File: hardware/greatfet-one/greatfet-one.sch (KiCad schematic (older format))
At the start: 99 parts, among them J1 NEIGHBOR1, J2 NEIGHBOR2, J3 USB-MICRO-B-SHIELDED, J4 USB-MICRO-B-SHIELDED, J5 JTAG, J6 POWER, J7 BONUS_ROW, SW1 DFU, SW2 RESET, U1 LPC4330FBD144, U2 W25Q16DV, U3 AP7333, U4 IP4220CZ6, U5 AP2553W6-7, X1 MCU_XTAL, X2 RTC_XTAL

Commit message: GreatFET One: replaced D5 with a part with lower forward voltage to maximize the usefulness of +5V for USB1 and neighbors
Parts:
- D5: footprint gsg-modules:B140-13-F -> gsg-modules:SOD128; Description DIODE SCHOTTKY 40V 1A SMA -> DIODE SCHOTTKY 30V 5A SOD128; Manufacturer Diodes Inc. -> NXP; Part Number B140-13-F -> PMEG3050EP,115
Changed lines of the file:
@@
 F 0 "D5" H 2500 6300 50  0000 C CNN
 F 1 "VBUS_DIODE" H 2500 6100 50  0000 C CNN
-F 2 "gsg-modules:B140-13-F" H 2500 6200 60  0001 C CNN
+F 2 "gsg-modules:SOD128" H 2500 6200 60  0001 C CNN
 F 3 "" H 2500 6200 60  0000 C CNN
-F 4 "Diodes Inc." H 2500 6200 60  0001 C CNN "Manufacturer"
-F 5 "B140-13-F" H 2500 6200 60  0001 C CNN "Part Number"
-F 6 "DIODE SCHOTTKY 40V 1A SMA" H 2500 6200 60  0001 C CNN "Description"
+F 4 "NXP" H 2500 6200 60  0001 C CNN "Manufacturer"
+F 5 "PMEG3050EP,115" H 2500 6200 60  0001 C CNN "Part Number"
+F 6 "DIODE SCHOTTKY 30V 5A SOD128 " H 2500 6200 60  0001 C CNN "Description"
 	1    2500 6200
 	1    0    0    -1

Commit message: GreatFET One: corrected part numbers for 18k resistors
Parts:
- R22, R26: Description RES SMD 10K OHM 5% 1/10W 0603 -> RES SMD 18K OHM 5% 1/10W 0603; Part Number RC0603JR-0710KL -> RC0603JR-0718KL
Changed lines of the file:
@@
 F 3 "" H 13200 4950 30  0000 C CNN
 F 4 "Yageo" H 13200 4950 60  0001 C CNN "Manufacturer"
-F 5 "RC0603JR-0710KL" H 13200 4950 60  0001 C CNN "Part Number"
-F 6 "RES SMD 10K OHM 5% 1/10W 0603" H 13200 4950 60  0001 C CNN "Description"
+F 5 "RC0603JR-0718KL" H 13200 4950 60  0001 C CNN "Part Number"
+F 6 "RES SMD 18K OHM 5% 1/10W 0603" H 13200 4950 60  0001 C CNN "Description"
 	1    13200 4950
 	-1   0    0    1
@@
 F 3 "" H 2800 7250 30  0000 C CNN
 F 4 "Yageo" H 2800 7250 60  0001 C CNN "Manufacturer"
-F 5 "RC0603JR-0710KL" H 2800 7250 60  0001 C CNN "Part Number"
-F 6 "RES SMD 10K OHM 5% 1/10W 0603" H 2800 7250 60  0001 C CNN "Description"
+F 5 "RC0603JR-0718KL" H 2800 7250 60  0001 C CNN "Part Number"
+F 6 "RES SMD 18K OHM 5% 1/10W 0603" H 2800 7250 60  0001 C CNN "Description"
 	1    2800 7250
 	-1   0    0    1

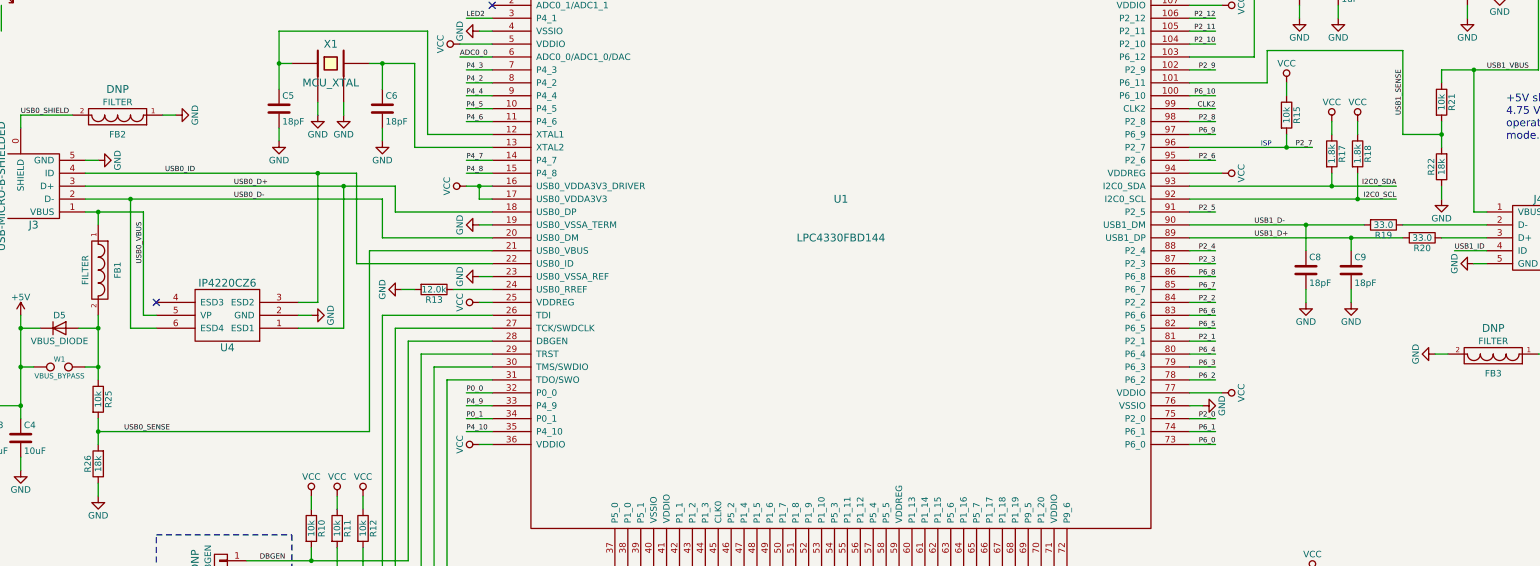
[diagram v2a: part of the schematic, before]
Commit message: GreatFET One: Changed resistor values to fix voltage dividers for USB0 and USB1 VBUS sensing.
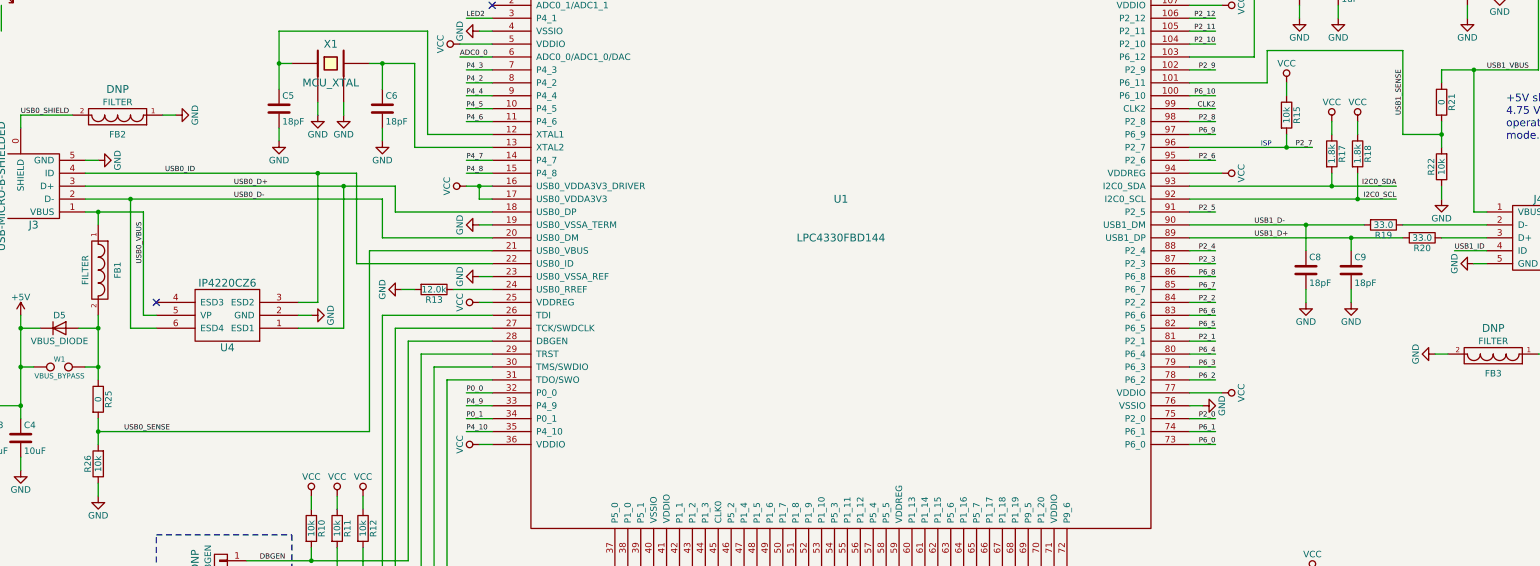
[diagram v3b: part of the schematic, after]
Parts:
- R21, R25: value 10k -> 0; Description RES 10K OHM 1/10W 5% 0603 SMD -> RES SMD 0.0OHM JUMPER 1/10W 0603; Manufacturer Panasonic -> Yageo; Part Number ERJ-3GEYJ103V -> RC0603JR-070RL
- R22, R26: value 18k -> 10k; Description RES SMD 18K OHM 5% 1/10W 0603 -> RES 10K OHM 1/10W 5% 0603 SMD; Manufacturer Yageo -> Panasonic; Part Number RC0603JR-0718KL -> ERJ-3GEYJ103V
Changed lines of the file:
@@
 P 13200 4950
 F 0 "R22" V 13280 4950 50  0000 C CNN
-F 1 "18k" V 13200 4950 50  0000 C CNN
+F 1 "10k" V 13200 4950 50  0000 C CNN
 F 2 "gsg-modules:0603" V 13130 4950 30  0001 C CNN
 F 3 "" H 13200 4950 30  0000 C CNN
-F 4 "Yageo" H 13200 4950 60  0001 C CNN "Manufacturer"
-F 5 "RC0603JR-0718KL" H 13200 4950 60  0001 C CNN "Part Number"
-F 6 "RES SMD 18K OHM 5% 1/10W 0603" H 13200 4950 60  0001 C CNN "Description"
+F 4 "Panasonic" H 13200 4950 60  0001 C CNN "Manufacturer"
+F 5 "ERJ-3GEYJ103V" H 13200 4950 60  0001 C CNN "Part Number"
+F 6 "RES 10K OHM 1/10W 5% 0603 SMD" H 13200 4950 60  0001 C CNN "Description"
 	1    13200 4950
 	-1   0    0    1
@@
 P 13200 4450
 F 0 "R21" V 13280 4450 50  0000 C CNN
-F 1 "10k" V 13200 4450 50  0000 C CNN
+F 1 "0" V 13200 4450 50  0000 C CNN
 F 2 "gsg-modules:0603" V 13130 4450 30  0001 C CNN
 F 3 "" H 13200 4450 30  0000 C CNN
-F 4 "Panasonic" H 13200 4450 60  0001 C CNN "Manufacturer"
-F 5 "ERJ-3GEYJ103V" H 13200 4450 60  0001 C CNN "Part Number"
-F 6 "RES 10K OHM 1/10W 5% 0603 SMD" H 13200 4450 60  0001 C CNN "Description"
+F 4 "Yageo" H 13200 4450 60  0001 C CNN "Manufacturer"
+F 5 "RC0603JR-070RL" H 13200 4450 60  0001 C CNN "Part Number"
+F 6 "RES SMD 0.0OHM JUMPER 1/10W 0603" H 13200 4450 60  0001 C CNN "Description"
 	1    13200 4450
 	1    0    0    -1
@@
 P 2800 6750
 F 0 "R25" V 2880 6750 50  0000 C CNN
-F 1 "10k" V 2800 6750 50  0000 C CNN
+F 1 "0" V 2800 6750 50  0000 C CNN
 F 2 "gsg-modules:0603" V 2730 6750 30  0001 C CNN
 F 3 "" H 2800 6750 30  0000 C CNN
-F 4 "Panasonic" H 2800 6750 60  0001 C CNN "Manufacturer"
-F 5 "ERJ-3GEYJ103V" H 2800 6750 60  0001 C CNN "Part Number"
-F 6 "RES 10K OHM 1/10W 5% 0603 SMD" H 2800 6750 60  0001 C CNN "Description"
+F 4 "Yageo" H 2800 6750 60  0001 C CNN "Manufacturer"
+F 5 "RC0603JR-070RL" H 2800 6750 60  0001 C CNN "Part Number"
+F 6 "RES SMD 0.0OHM JUMPER 1/10W 0603" H 2800 6750 60  0001 C CNN "Description"
 	1    2800 6750
 	1    0    0    -1
@@
 P 2800 7250
 F 0 "R26" V 2880 7250 50  0000 C CNN
-F 1 "18k" V 2800 7250 50  0000 C CNN
+F 1 "10k" V 2800 7250 50  0000 C CNN
 F 2 "gsg-modules:0603" V 2730 7250 30  0001 C CNN
 F 3 "" H 2800 7250 30  0000 C CNN
-F 4 "Yageo" H 2800 7250 60  0001 C CNN "Manufacturer"
-F 5 "RC0603JR-0718KL" H 2800 7250 60  0001 C CNN "Part Number"
-F 6 "RES SMD 18K OHM 5% 1/10W 0603" H 2800 7250 60  0001 C CNN "Description"
+F 4 "Panasonic" H 2800 7250 60  0001 C CNN "Manufacturer"
+F 5 "ERJ-3GEYJ103V" H 2800 7250 60  0001 C CNN "Part Number"
+F 6 "RES 10K OHM 1/10W 5% 0603 SMD" H 2800 7250 60  0001 C CNN "Description"
 	1    2800 7250
 	-1   0    0    1

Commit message: Restored VBUS voltage dividers which work correctly now that we learned how to turn off VBUS discharge in the microcontroller.
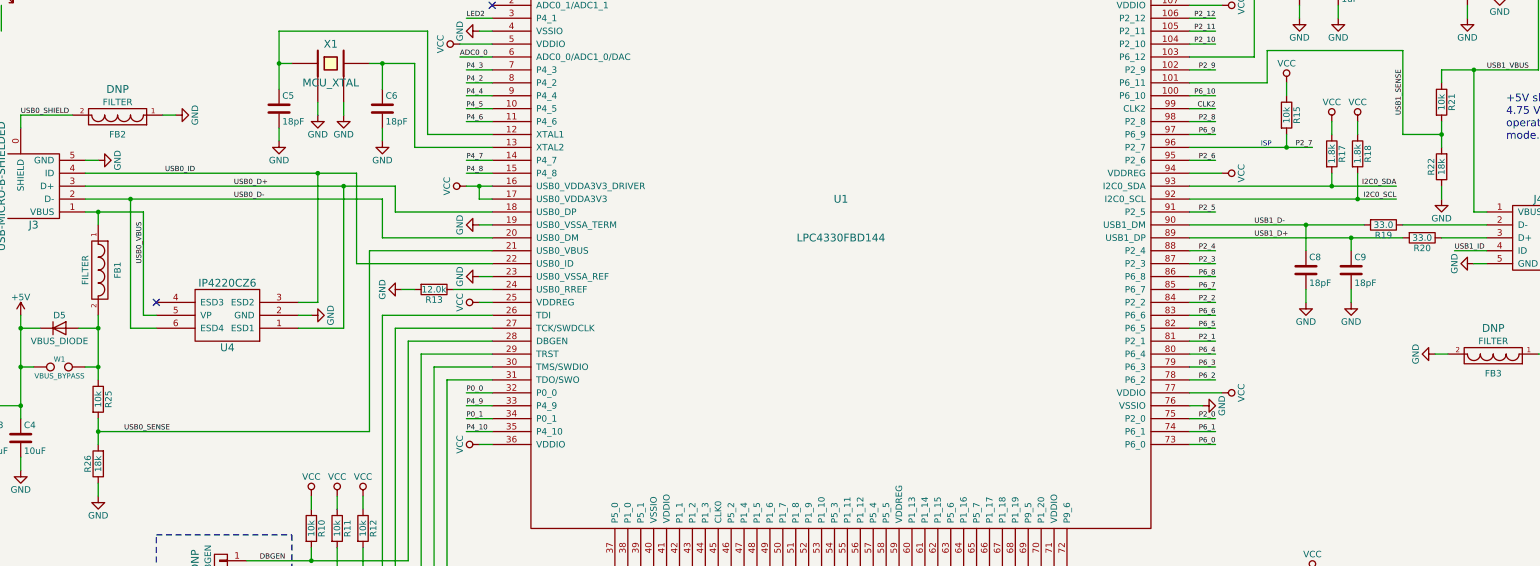
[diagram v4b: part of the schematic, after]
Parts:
- R21, R25: value 0 -> 10k; Description RES SMD 0.0OHM JUMPER 1/10W 0603 -> RES 10K OHM 1/10W 5% 0603 SMD; Manufacturer Yageo -> Panasonic; Part Number RC0603JR-070RL -> ERJ-3GEYJ103V
- R22, R26: value 10k -> 18k; Description RES 10K OHM 1/10W 5% 0603 SMD -> RES SMD 18K OHM 5% 1/10W 0603; Manufacturer Panasonic -> Yageo; Part Number ERJ-3GEYJ103V -> RC0603JR-0718KL
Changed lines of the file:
@@
 P 13200 4950
 F 0 "R22" V 13280 4950 50  0000 C CNN
-F 1 "10k" V 13200 4950 50  0000 C CNN
+F 1 "18k" V 13200 4950 50  0000 C CNN
 F 2 "gsg-modules:0603" V 13130 4950 30  0001 C CNN
 F 3 "" H 13200 4950 30  0000 C CNN
-F 4 "Panasonic" H 13200 4950 60  0001 C CNN "Manufacturer"
-F 5 "ERJ-3GEYJ103V" H 13200 4950 60  0001 C CNN "Part Number"
-F 6 "RES 10K OHM 1/10W 5% 0603 SMD" H 13200 4950 60  0001 C CNN "Description"
+F 4 "Yageo" H 13200 4950 60  0001 C CNN "Manufacturer"
+F 5 "RC0603JR-0718KL" H 13200 4950 60  0001 C CNN "Part Number"
+F 6 "RES SMD 18K OHM 5% 1/10W 0603" H 13200 4950 60  0001 C CNN "Description"
 	1    13200 4950
 	-1   0    0    1
@@
 P 13200 4450
 F 0 "R21" V 13280 4450 50  0000 C CNN
-F 1 "0" V 13200 4450 50  0000 C CNN
+F 1 "10k" V 13200 4450 50  0000 C CNN
 F 2 "gsg-modules:0603" V 13130 4450 30  0001 C CNN
 F 3 "" H 13200 4450 30  0000 C CNN
-F 4 "Yageo" H 13200 4450 60  0001 C CNN "Manufacturer"
-F 5 "RC0603JR-070RL" H 13200 4450 60  0001 C CNN "Part Number"
-F 6 "RES SMD 0.0OHM JUMPER 1/10W 0603" H 13200 4450 60  0001 C CNN "Description"
+F 4 "Panasonic" H 13200 4450 60  0001 C CNN "Manufacturer"
+F 5 "ERJ-3GEYJ103V" H 13200 4450 60  0001 C CNN "Part Number"
+F 6 "RES 10K OHM 1/10W 5% 0603 SMD" H 13200 4450 60  0001 C CNN "Description"
 	1    13200 4450
 	1    0    0    -1
@@
 P 2800 6750
 F 0 "R25" V 2880 6750 50  0000 C CNN
-F 1 "0" V 2800 6750 50  0000 C CNN
+F 1 "10k" V 2800 6750 50  0000 C CNN
 F 2 "gsg-modules:0603" V 2730 6750 30  0001 C CNN
 F 3 "" H 2800 6750 30  0000 C CNN
-F 4 "Yageo" H 2800 6750 60  0001 C CNN "Manufacturer"
-F 5 "RC0603JR-070RL" H 2800 6750 60  0001 C CNN "Part Number"
-F 6 "RES SMD 0.0OHM JUMPER 1/10W 0603" H 2800 6750 60  0001 C CNN "Description"
+F 4 "Panasonic" H 2800 6750 60  0001 C CNN "Manufacturer"
+F 5 "ERJ-3GEYJ103V" H 2800 6750 60  0001 C CNN "Part Number"
+F 6 "RES 10K OHM 1/10W 5% 0603 SMD" H 2800 6750 60  0001 C CNN "Description"
 	1    2800 6750
 	1    0    0    -1
@@
 P 2800 7250
 F 0 "R26" V 2880 7250 50  0000 C CNN
-F 1 "10k" V 2800 7250 50  0000 C CNN
+F 1 "18k" V 2800 7250 50  0000 C CNN
 F 2 "gsg-modules:0603" V 2730 7250 30  0001 C CNN
 F 3 "" H 2800 7250 30  0000 C CNN
-F 4 "Panasonic" H 2800 7250 60  0001 C CNN "Manufacturer"
-F 5 "ERJ-3GEYJ103V" H 2800 7250 60  0001 C CNN "Part Number"
-F 6 "RES 10K OHM 1/10W 5% 0603 SMD" H 2800 7250 60  0001 C CNN "Description"
+F 4 "Yageo" H 2800 7250 60  0001 C CNN "Manufacturer"
+F 5 "RC0603JR-0718KL" H 2800 7250 60  0001 C CNN "Part Number"
+F 6 "RES SMD 18K OHM 5% 1/10W 0603" H 2800 7250 60  0001 C CNN "Description"
 	1    2800 7250
 	-1   0    0    1

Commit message: updated from discontinued W25Q16DVSSIG to compatible W25Q16JVSSIQ
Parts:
- U2: Part Number W25Q16DVSSIG -> W25Q16JVSSIQ
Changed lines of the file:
@@
 F 3 "" H 10550 1800 60  0000 C CNN
 F 4 "Winbond" H 10550 1800 60  0001 C CNN "Manufacturer"
-F 5 "W25Q16DVSSIG" H 10550 1800 60  0001 C CNN "Part Number"
+F 5 "W25Q16JVSSIQ" H 10550 1800 60  0001 C CNN "Part Number"
 F 6 "IC FLASH 16MBIT 104MHZ 8SOIC" H 10550 1800 60  0001 C CNN "Description"
 	1    10550 1800

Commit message: GreatFET One: updated schematic symbols to newer kicad library
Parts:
- W1: symbol TEST -> TEST_2P
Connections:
- net LED1: now also D1.1 (K)
- net LED2: now also D2.1 (K)
- net LED3: now also D3.1 (K)
- net LED4: now also D4.1 (K)
- net at D1.2 (A): now also R1.2
- net at D2.2 (A): now also R2.2
- net at D3.2 (A): now also R3.2
- net at D4.2 (A): now also R4.2
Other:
- moved on the sheet: D1, D2, D3, D4
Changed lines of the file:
@@
 EESchema Schematic File Version 2
+LIBS:greatfet-one-rescue
 LIBS:power
 LIBS:device
@@
 L LED D1
 U 1 1 55E38B6A
-P 1150 3500
-F 0 "D1" H 1150 3600 50  0000 C CNN
-F 1 "LED1" H 1150 3400 50  0000 C CNN
-F 2 "gsg-modules:0603D" H 1150 3500 60  0001 C CNN
-F 3 "" H 1150 3500 60  0000 C CNN
-F 4 "Lumex" H 1150 3500 60  0001 C CNN "Manufacturer"
-F 5 "SML-LX0603GW-TR" H 1150 3500 60  0001 C CNN "Part Number"
-F 6 "LED GREEN DIFFUSED 0603 SMD" H 1150 3500 60  0001 C CNN "Description"
-	1    1150 3500
+P 1150 3450
+F 0 "D1" H 1150 3550 50  0000 C CNN
+F 1 "LED1" H 1150 3350 50  0000 C CNN
+F 2 "gsg-modules:0603D" H 1150 3450 60  0001 C CNN
+F 3 "" H 1150 3450 60  0000 C CNN
+F 4 "Lumex" H 1150 3450 60  0001 C CNN "Manufacturer"
+F 5 "SML-LX0603GW-TR" H 1150 3450 60  0001 C CNN "Part Number"
+F 6 "LED GREEN DIFFUSED 0603 SMD" H 1150 3450 60  0001 C CNN "Description"
+	1    1150 3450
 	0    -1   -1   0
 $EndComp
@@
 L LED D2
 U 1 1 55E7AAAC
-P 1450 3500
-F 0 "D2" H 1450 3600 50  0000 C CNN
-F 1 "LED2" H 1450 3400 50  0000 C CNN
-F 2 "gsg-modules:0603D" H 1450 3500 60  0001 C CNN
-F 3 "" H 1450 3500 60  0000 C CNN
-F 4 "Lumex" H 1450 3500 60  0001 C CNN "Manufacturer"
-F 5 "SML-LX0603YW-TR" H 1450 3500 60  0001 C CNN "Part Number"
-F 6 "LED YELLOW DIFFUSED 0603 SMD" H 1450 3500 60  0001 C CNN "Description"
-	1    1450 3500
+P 1450 3450
+F 0 "D2" H 1450 3550 50  0000 C CNN
+F 1 "LED2" H 1450 3350 50  0000 C CNN
+F 2 "gsg-modules:0603D" H 1450 3450 60  0001 C CNN
+F 3 "" H 1450 3450 60  0000 C CNN
+F 4 "Lumex" H 1450 3450 60  0001 C CNN "Manufacturer"
+F 5 "SML-LX0603YW-TR" H 1450 3450 60  0001 C CNN "Part Number"
+F 6 "LED YELLOW DIFFUSED 0603 SMD" H 1450 3450 60  0001 C CNN "Description"
+	1    1450 3450
 	0    -1   -1   0
 $EndComp
@@
 L LED D3
 U 1 1 55E7AC50
-P 1750 3500
-F 0 "D3" H 1750 3600 50  0000 C CNN
-F 1 "LED3" H 1750 3400 50  0000 C CNN
-F 2 "gsg-modules:0603D" H 1750 3500 60  0001 C CNN
-F 3 "" H 1750 3500 60  0000 C CNN
-F 4 "Lumex" H 1750 3500 60  0001 C CNN "Manufacturer"
-F 5 "SML-LX0603GW-TR" H 1750 3500 60  0001 C CNN "Part Number"
-F 6 "LED GREEN DIFFUSED 0603 SMD" H 1750 3500 60  0001 C CNN "Description"
-	1    1750 3500
+P 1750 3450
+F 0 "D3" H 1750 3550 50  0000 C CNN
+F 1 "LED3" H 1750 3350 50  0000 C CNN
+F 2 "gsg-modules:0603D" H 1750 3450 60  0001 C CNN
+F 3 "" H 1750 3450 60  0000 C CNN
+F 4 "Lumex" H 1750 3450 60  0001 C CNN "Manufacturer"
+F 5 "SML-LX0603GW-TR" H 1750 3450 60  0001 C CNN "Part Number"
+F 6 "LED GREEN DIFFUSED 0603 SMD" H 1750 3450 60  0001 C CNN "Description"
+	1    1750 3450
 	0    -1   -1   0
 $EndComp
@@
 L LED D4
 U 1 1 55E7AC6E
-P 2050 3500
-F 0 "D4" H 2050 3600 50  0000 C CNN
-F 1 "LED4" H 2050 3400 50  0000 C CNN
-F 2 "gsg-modules:0603D" H 2050 3500 60  0001 C CNN
-F 3 "" H 2050 3500 60  0000 C CNN
-F 4 "Lumex" H 2050 3500 60  0001 C CNN "Manufacturer"
-F 5 "SML-LX0603YW-TR" H 2050 3500 60  0001 C CNN "Part Number"
-F 6 "LED YELLOW DIFFUSED 0603 SMD" H 2050 3500 60  0001 C CNN "Description"
-	1    2050 3500
+P 2050 3450
+F 0 "D4" H 2050 3550 50  0000 C CNN
+F 1 "LED4" H 2050 3350 50  0000 C CNN
+F 2 "gsg-modules:0603D" H 2050 3450 60  0001 C CNN
+F 3 "" H 2050 3450 60  0000 C CNN
+F 4 "Lumex" H 2050 3450 60  0001 C CNN "Manufacturer"
+F 5 "SML-LX0603YW-TR" H 2050 3450 60  0001 C CNN "Part Number"
+F 6 "LED YELLOW DIFFUSED 0603 SMD" H 2050 3450 60  0001 C CNN "Description"
+	1    2050 3450
 	0    -1   -1   0
 $EndComp
@@
 	1    0    0    -1
 $EndComp
-Text Label 1750 3900 1    40   ~ 0
+Text Label 1750 3800 1    40   ~ 0
 LED3
-Text Label 2050 3900 1    40   ~ 0
+Text Label 2050 3800 1    40   ~ 0
 LED4
-Text Label 1150 3900 1    40   ~ 0
+Text Label 1150 3800 1    40   ~ 0
 LED1
-Text Label 1450 3900 1    40   ~ 0
+Text Label 1450 3800 1    40   ~ 0
 LED2
 $Comp
@@
 	1150 3200 1150 3300
 Wire Wire Line
-	1150 3700 1150 3900
+	1150 3600 1150 3800
 Wire Wire Line
 	1450 2800 1450 2900
@@
 	1450 3200 1450 3300
 Wire Wire Line
-	1450 3700 1450 3900
+	1450 3600 1450 3800
 Wire Wire Line
 	1750 2800 1750 2900
@@
 	1750 3200 1750 3300
 Wire Wire Line
-	1750 3700 1750 3900
+	1750 3600 1750 3800
 Wire Wire Line
 	2050 2800 2050 2900
@@
 	2050 3200 2050 3300
 Wire Wire Line
-	2050 3700 2050 3900
+	2050 3600 2050 3800
 Wire Wire Line
 	15300 4300 15500 4300
@@
 	5750 1200 6100 1200
 $Comp
-L TEST W1
+L TEST_2P W1
 U 1 1 57C655EF
 P 2500 6500
